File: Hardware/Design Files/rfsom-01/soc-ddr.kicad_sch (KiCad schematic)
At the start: 64 parts, among them U5 XC7Z010-1CLG400C

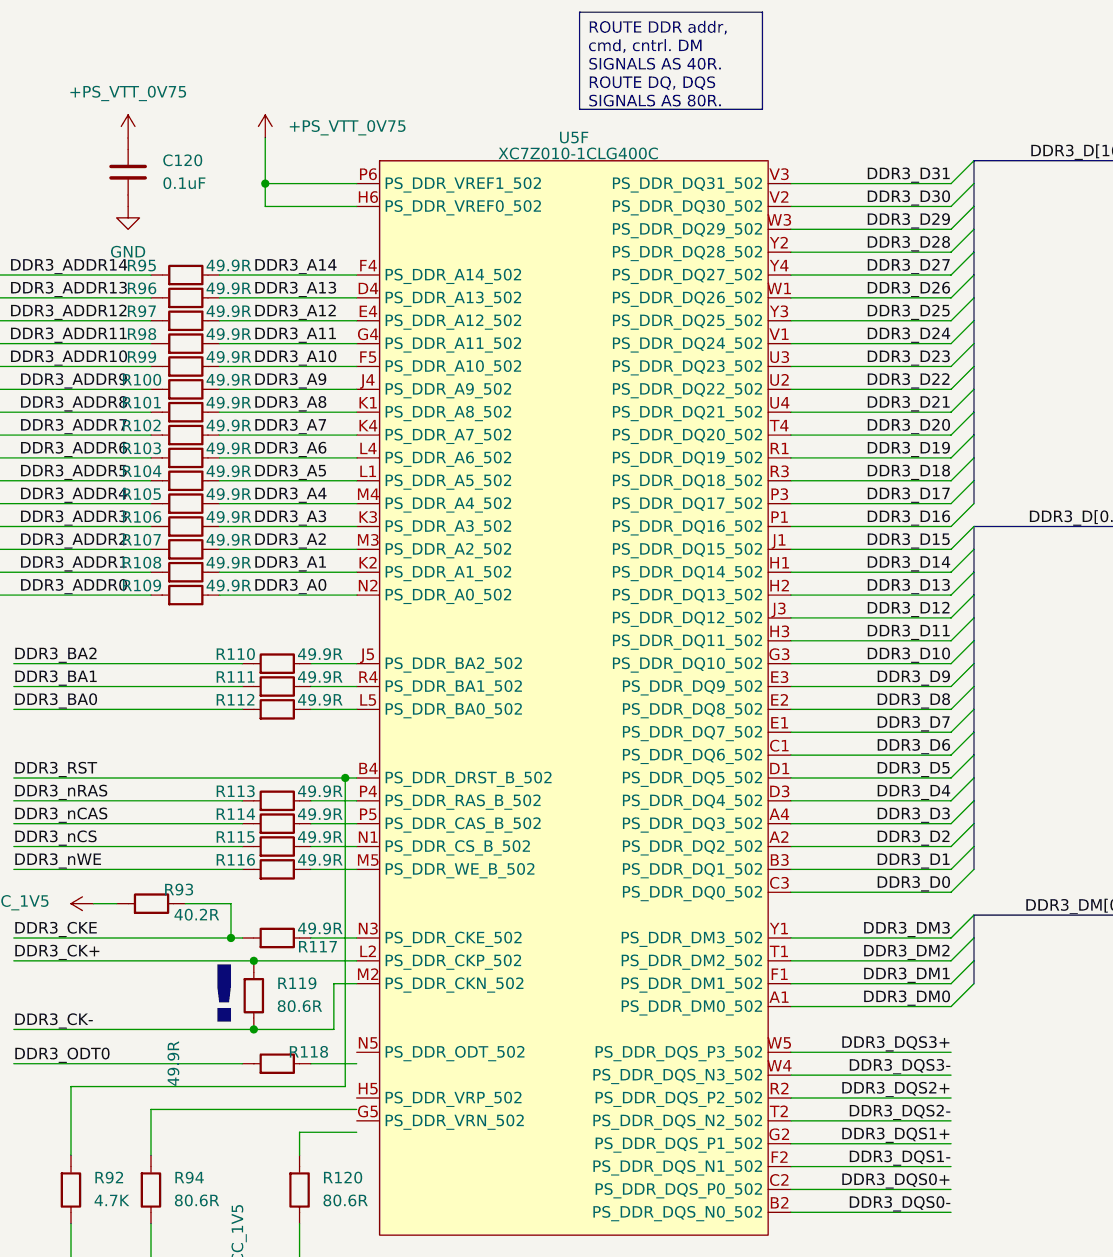
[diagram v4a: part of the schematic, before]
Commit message: routing changes; added mezzanine; added pl ram;
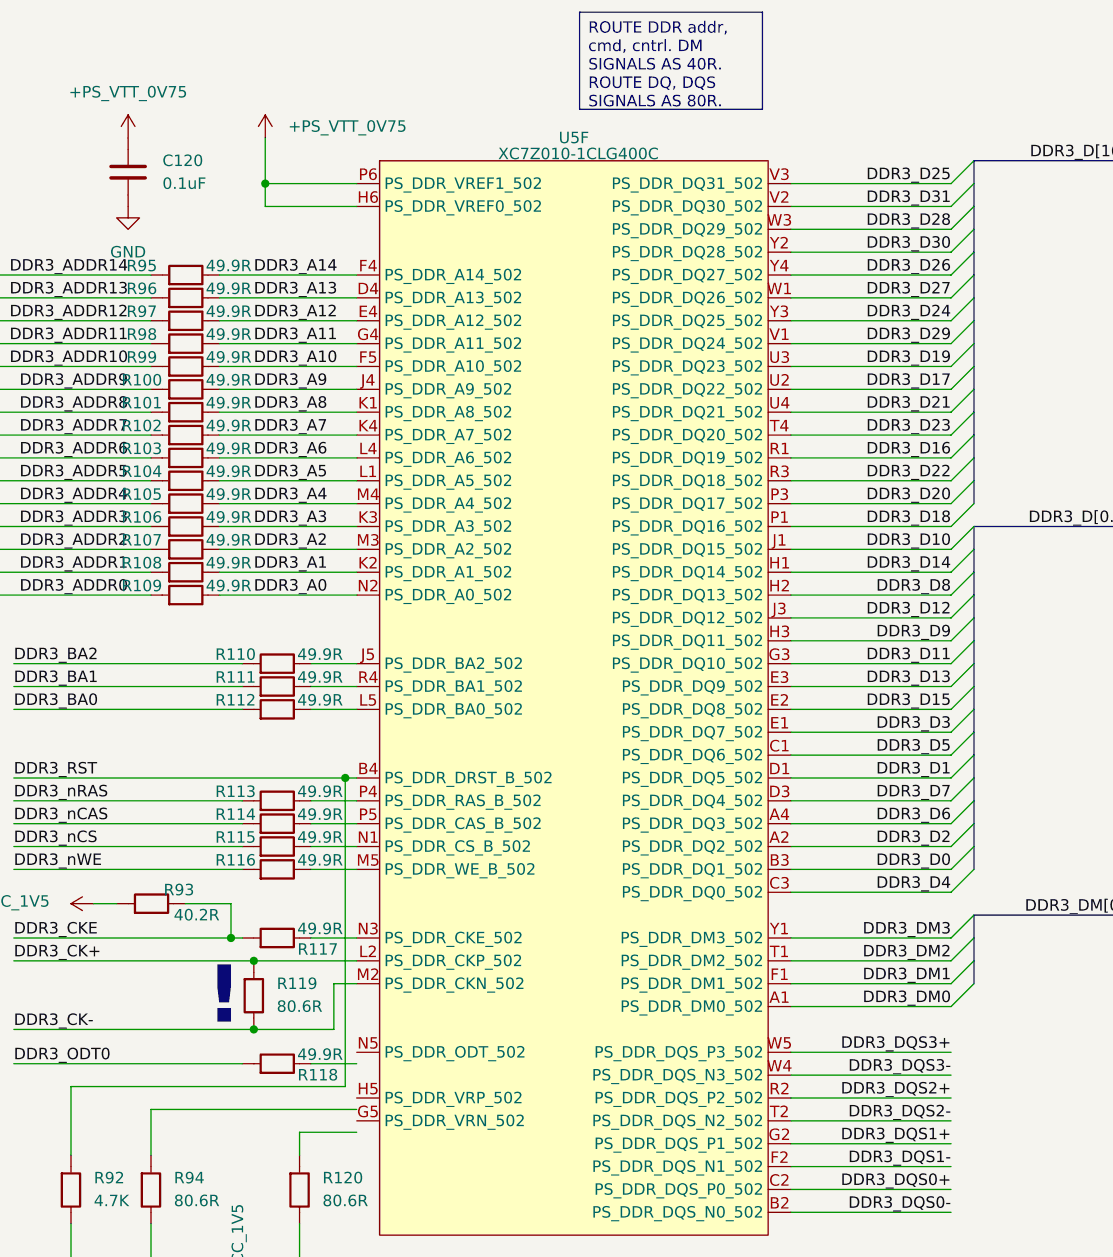
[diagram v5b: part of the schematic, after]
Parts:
- R100, R101, R102, R103, R104, R105, R106, R107, R108, R109, R110, R111, R112, R113, R114, R115, R116, R117, R118, R95, R96, R97, R98, R99: footprint Resistor_SMD:R_0603_1608Metric -> Resistor_SMD:R_0402_1005Metric_Pad0.72x0.64mm_HandSolder; symbol Resistors:RC0603FR-0749R9L -> Resistors:RC0402FR-0749R9L
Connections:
- net DDR3_D0: now also U5.B3 (PS_DDR_DQ1_502); no longer U5.C3 (PS_DDR_DQ0_502)
- net DDR3_D1: now also U5.D1 (PS_DDR_DQ5_502); no longer U5.B3 (PS_DDR_DQ1_502)
- net DDR3_D10: now also U5.J1 (PS_DDR_DQ15_502); no longer U5.G3 (PS_DDR_DQ10_502)
- net DDR3_D11: now also U5.G3 (PS_DDR_DQ10_502); no longer U5.H3 (PS_DDR_DQ11_502)
- net DDR3_D13: now also U5.E3 (PS_DDR_DQ9_502); no longer U5.H2 (PS_DDR_DQ13_502)
- net DDR3_D15: now also U5.E2 (PS_DDR_DQ8_502); no longer U5.J1 (PS_DDR_DQ15_502)
- net DDR3_D16: now also U5.R1 (PS_DDR_DQ19_502); no longer U5.P1 (PS_DDR_DQ16_502)
- net DDR3_D17: now also U5.U2 (PS_DDR_DQ22_502); no longer U5.P3 (PS_DDR_DQ17_502)
- net DDR3_D18: now also U5.P1 (PS_DDR_DQ16_502); no longer U5.R3 (PS_DDR_DQ18_502)
- net DDR3_D19: now also U5.U3 (PS_DDR_DQ23_502); no longer U5.R1 (PS_DDR_DQ19_502)
- net DDR3_D20: now also U5.P3 (PS_DDR_DQ17_502); no longer U5.T4 (PS_DDR_DQ20_502)
- net DDR3_D22: now also U5.R3 (PS_DDR_DQ18_502); no longer U5.U2 (PS_DDR_DQ22_502)
- net DDR3_D23: now also U5.T4 (PS_DDR_DQ20_502); no longer U5.U3 (PS_DDR_DQ23_502)
- net DDR3_D24: now also U5.Y3 (PS_DDR_DQ25_502); no longer U5.V1 (PS_DDR_DQ24_502)
- net DDR3_D25: now also U5.V3 (PS_DDR_DQ31_502); no longer U5.Y3 (PS_DDR_DQ25_502)
- net DDR3_D26: now also U5.Y4 (PS_DDR_DQ27_502); no longer U5.W1 (PS_DDR_DQ26_502)
- net DDR3_D27: now also U5.W1 (PS_DDR_DQ26_502); no longer U5.Y4 (PS_DDR_DQ27_502)
- net DDR3_D28: now also U5.W3 (PS_DDR_DQ29_502); no longer U5.Y2 (PS_DDR_DQ28_502)
- net DDR3_D29: now also U5.V1 (PS_DDR_DQ24_502); no longer U5.W3 (PS_DDR_DQ29_502)
- net DDR3_D3: now also U5.E1 (PS_DDR_DQ7_502); no longer U5.A4 (PS_DDR_DQ3_502)
- net DDR3_D30: now also U5.Y2 (PS_DDR_DQ28_502); no longer U5.V2 (PS_DDR_DQ30_502)
- net DDR3_D31: now also U5.V2 (PS_DDR_DQ30_502); no longer U5.V3 (PS_DDR_DQ31_502)
- net DDR3_D4: now also U5.C3 (PS_DDR_DQ0_502); no longer U5.D3 (PS_DDR_DQ4_502)
- net DDR3_D5: now also U5.C1 (PS_DDR_DQ6_502); no longer U5.D1 (PS_DDR_DQ5_502)
- net DDR3_D6: now also U5.A4 (PS_DDR_DQ3_502); no longer U5.C1 (PS_DDR_DQ6_502)
- net DDR3_D7: now also U5.D3 (PS_DDR_DQ4_502); no longer U5.E1 (PS_DDR_DQ7_502)
- net DDR3_D8: now also U5.H2 (PS_DDR_DQ13_502); no longer U5.E2 (PS_DDR_DQ8_502)
- net DDR3_D9: now also U5.H3 (PS_DDR_DQ11_502); no longer U5.E3 (PS_DDR_DQ9_502)

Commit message: replaced pmic;
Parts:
- R100, R101, R102, R103, R104, R105, R106, R107, R108, R109, R110, R111, R112, R113, R114, R115, R116, R117, R118, R95, R96, R97, R98, R99: footprint Resistor_SMD:R_0402_1005Metric_Pad0.72x0.64mm_HandSolder -> Resistor_SMD:R_0402_1005Metric
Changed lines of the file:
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@@
 			)
 		)
-		(property "Footprint" "Resistor_SMD:R_0402_1005Metric_Pad0.72x0.64mm_HandSolder"
+		(property "Footprint" "Resistor_SMD:R_0402_1005Metric"
 			(at 167.64 53.34 0)
 			(effects
@@
 			)
 		)
-		(property "Footprint" "Resistor_SMD:R_0402_1005Metric_Pad0.72x0.64mm_HandSolder"
+		(property "Footprint" "Resistor_SMD:R_0402_1005Metric"
 			(at 167.64 81.28 0)
 			(effects
@@
 			)
 		)
-		(property "Footprint" "Resistor_SMD:R_0402_1005Metric_Pad0.72x0.64mm_HandSolder"
+		(property "Footprint" "Resistor_SMD:R_0402_1005Metric"
 			(at 167.64 48.26 0)
 			(effects
@@
 			)
 		)
-		(property "Footprint" "Resistor_SMD:R_0402_1005Metric_Pad0.72x0.64mm_HandSolder"
+		(property "Footprint" "Resistor_SMD:R_0402_1005Metric"
 			(at 167.64 71.12 0)
 			(effects
@@
 			)
 		)
-		(property "Footprint" "Resistor_SMD:R_0402_1005Metric_Pad0.72x0.64mm_HandSolder"
+		(property "Footprint" "Resistor_SMD:R_0402_1005Metric"
 			(at 167.64 66.04 0)
 			(effects
@@
 			)
 		)
-		(property "Footprint" "Resistor_SMD:R_0402_1005Metric_Pad0.72x0.64mm_HandSolder"
+		(property "Footprint" "Resistor_SMD:R_0402_1005Metric"
 			(at 167.64 68.58 0)
 			(effects
@@
 			)
 		)
-		(property "Footprint" "Resistor_SMD:R_0402_1005Metric_Pad0.72x0.64mm_HandSolder"
+		(property "Footprint" "Resistor_SMD:R_0402_1005Metric"
 			(at 167.64 76.2 0)
 			(effects
@@
 			)
 		)
-		(property "Footprint" "Resistor_SMD:R_0402_1005Metric_Pad0.72x0.64mm_HandSolder"
+		(property "Footprint" "Resistor_SMD:R_0402_1005Metric"
 			(at 177.8 109.22 0)
 			(effects
@@
 			)
 		)
-		(property "Footprint" "Resistor_SMD:R_0402_1005Metric_Pad0.72x0.64mm_HandSolder"
+		(property "Footprint" "Resistor_SMD:R_0402_1005Metric"
 			(at 177.8 91.44 0)
 			(effects
@@
 			)
 		)
-		(property "Footprint" "Resistor_SMD:R_0402_1005Metric_Pad0.72x0.64mm_HandSolder"
+		(property "Footprint" "Resistor_SMD:R_0402_1005Metric"
 			(at 167.64 60.96 0)
 			(effects
@@
 			)
 		)
-		(property "Footprint" "Resistor_SMD:R_0402_1005Metric_Pad0.72x0.64mm_HandSolder"
+		(property "Footprint" "Resistor_SMD:R_0402_1005Metric"
 			(at 167.64 50.8 0)
 			(effects
@@
 			)
 		)
-		(property "Footprint" "Resistor_SMD:R_0402_1005Metric_Pad0.72x0.64mm_HandSolder"
+		(property "Footprint" "Resistor_SMD:R_0402_1005Metric"
 			(at 177.8 104.14 0)
 			(effects
@@
 			)
 		)
-		(property "Footprint" "Resistor_SMD:R_0402_1005Metric_Pad0.72x0.64mm_HandSolder"
+		(property "Footprint" "Resistor_SMD:R_0402_1005Metric"
 			(at 177.8 119.38 0)
 			(effects
@@
 			)
 		)
-		(property "Footprint" "Resistor_SMD:R_0402_1005Metric_Pad0.72x0.64mm_HandSolder"
+		(property "Footprint" "Resistor_SMD:R_0402_1005Metric"
 			(at 167.64 45.72 0)
 			(effects
@@
 			)
 		)
-		(property "Footprint" "Resistor_SMD:R_0402_1005Metric_Pad0.72x0.64mm_HandSolder"
+		(property "Footprint" "Resistor_SMD:R_0402_1005Metric"
 			(at 177.8 93.98 0)
 			(effects
@@
 			)
 		)
-		(property "Footprint" "Resistor_SMD:R_0402_1005Metric_Pad0.72x0.64mm_HandSolder"
+		(property "Footprint" "Resistor_SMD:R_0402_1005Metric"
 			(at 167.64 58.42 0)
 			(effects
@@
 			)
 		)
-		(property "Footprint" "Resistor_SMD:R_0402_1005Metric_Pad0.72x0.64mm_HandSolder"
+		(property "Footprint" "Resistor_SMD:R_0402_1005Metric"
 			(at 167.64 55.88 0)
 			(effects
@@
 			)
 		)
-		(property "Footprint" "Resistor_SMD:R_0402_1005Metric_Pad0.72x0.64mm_HandSolder"
+		(property "Footprint" "Resistor_SMD:R_0402_1005Metric"
 			(at 167.64 78.74 0)
 			(effects
@@
 			)
 		)
-		(property "Footprint" "Resistor_SMD:R_0402_1005Metric_Pad0.72x0.64mm_HandSolder"
+		(property "Footprint" "Resistor_SMD:R_0402_1005Metric"
 			(at 177.8 133.35 0)
 			(effects
@@
 			)
 		)
-		(property "Footprint" "Resistor_SMD:R_0402_1005Metric_Pad0.72x0.64mm_HandSolder"
+		(property "Footprint" "Resistor_SMD:R_0402_1005Metric"
 			(at 177.8 106.68 0)
 			(effects
@@
 			)
 		)
-		(property "Footprint" "Resistor_SMD:R_0402_1005Metric_Pad0.72x0.64mm_HandSolder"
+		(property "Footprint" "Resistor_SMD:R_0402_1005Metric"
 			(at 177.8 111.76 0)
 			(effects
@@
 			)
 		)
-		(property "Footprint" "Resistor_SMD:R_0402_1005Metric_Pad0.72x0.64mm_HandSolder"
+		(property "Footprint" "Resistor_SMD:R_0402_1005Metric"
 			(at 167.64 63.5 0)
 			(effects
@@
 			)
 		)
-		(property "Footprint" "Resistor_SMD:R_0402_1005Metric_Pad0.72x0.64mm_HandSolder"
+		(property "Footprint" "Resistor_SMD:R_0402_1005Metric"
 			(at 177.8 88.9 0)
 			(effects
@@
 			)
 		)
-		(property "Footprint" "Resistor_SMD:R_0402_1005Metric_Pad0.72x0.64mm_HandSolder"
+		(property "Footprint" "Resistor_SMD:R_0402_1005Metric"
 			(at 167.64 73.66 0)
 			(effects
